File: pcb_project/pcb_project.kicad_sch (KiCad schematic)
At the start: 0 parts

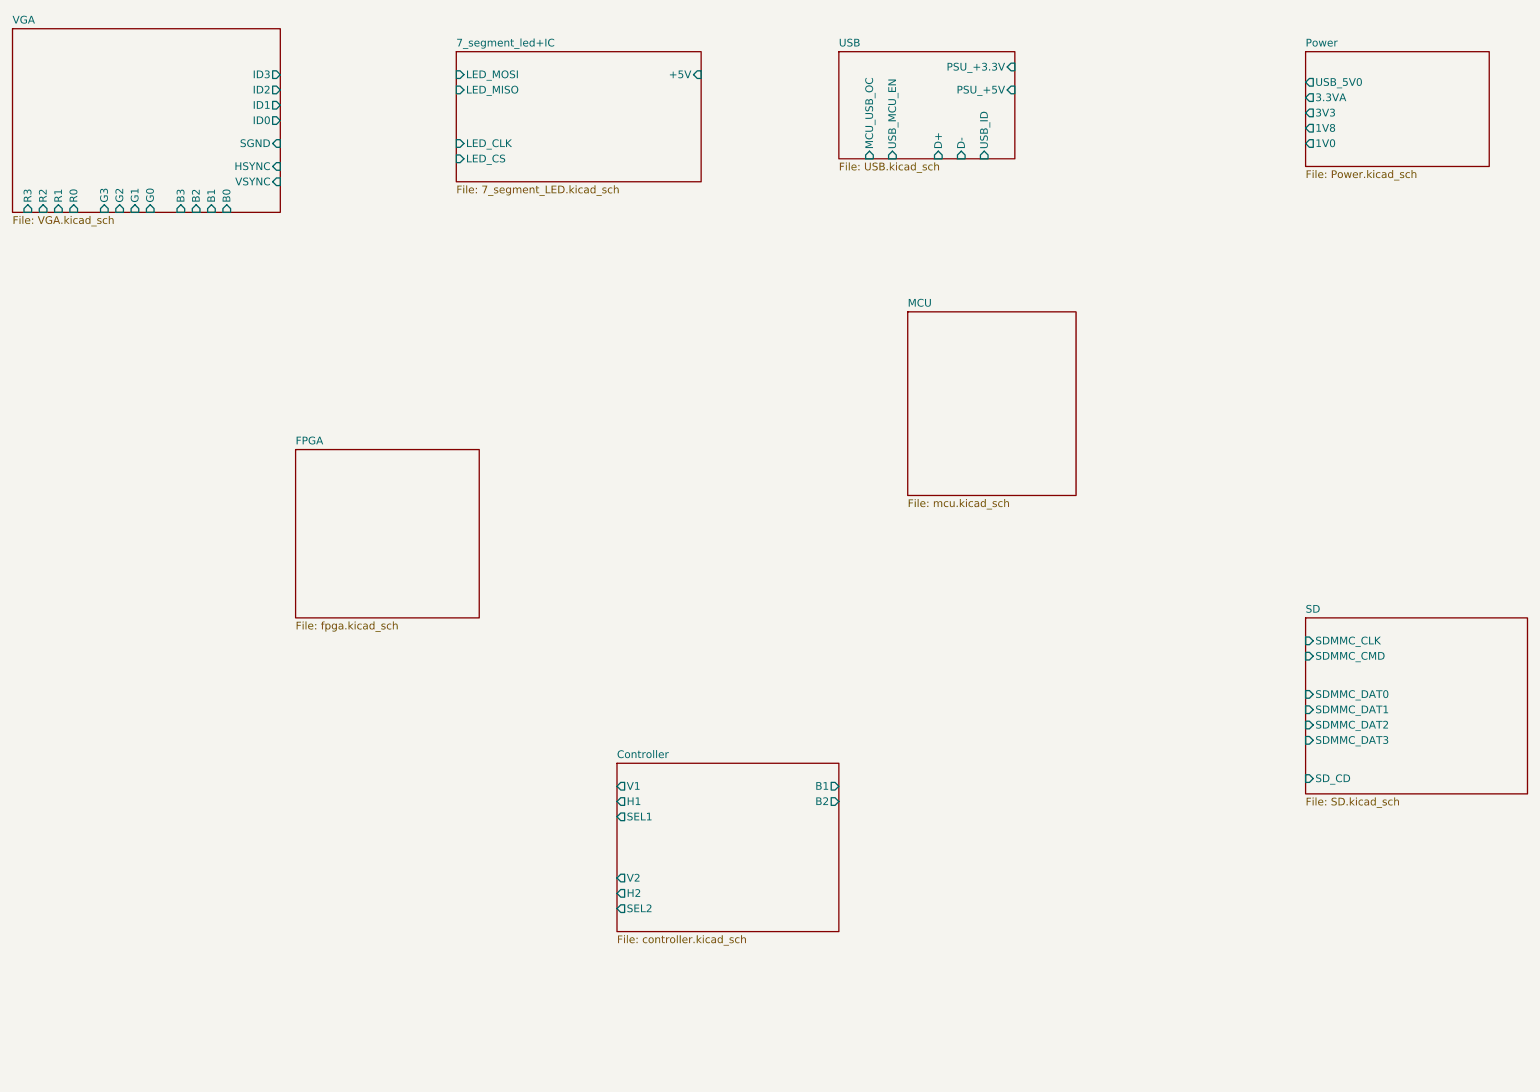
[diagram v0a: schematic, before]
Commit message: Connect Controller, LED-display, USB and SD reader to MCU
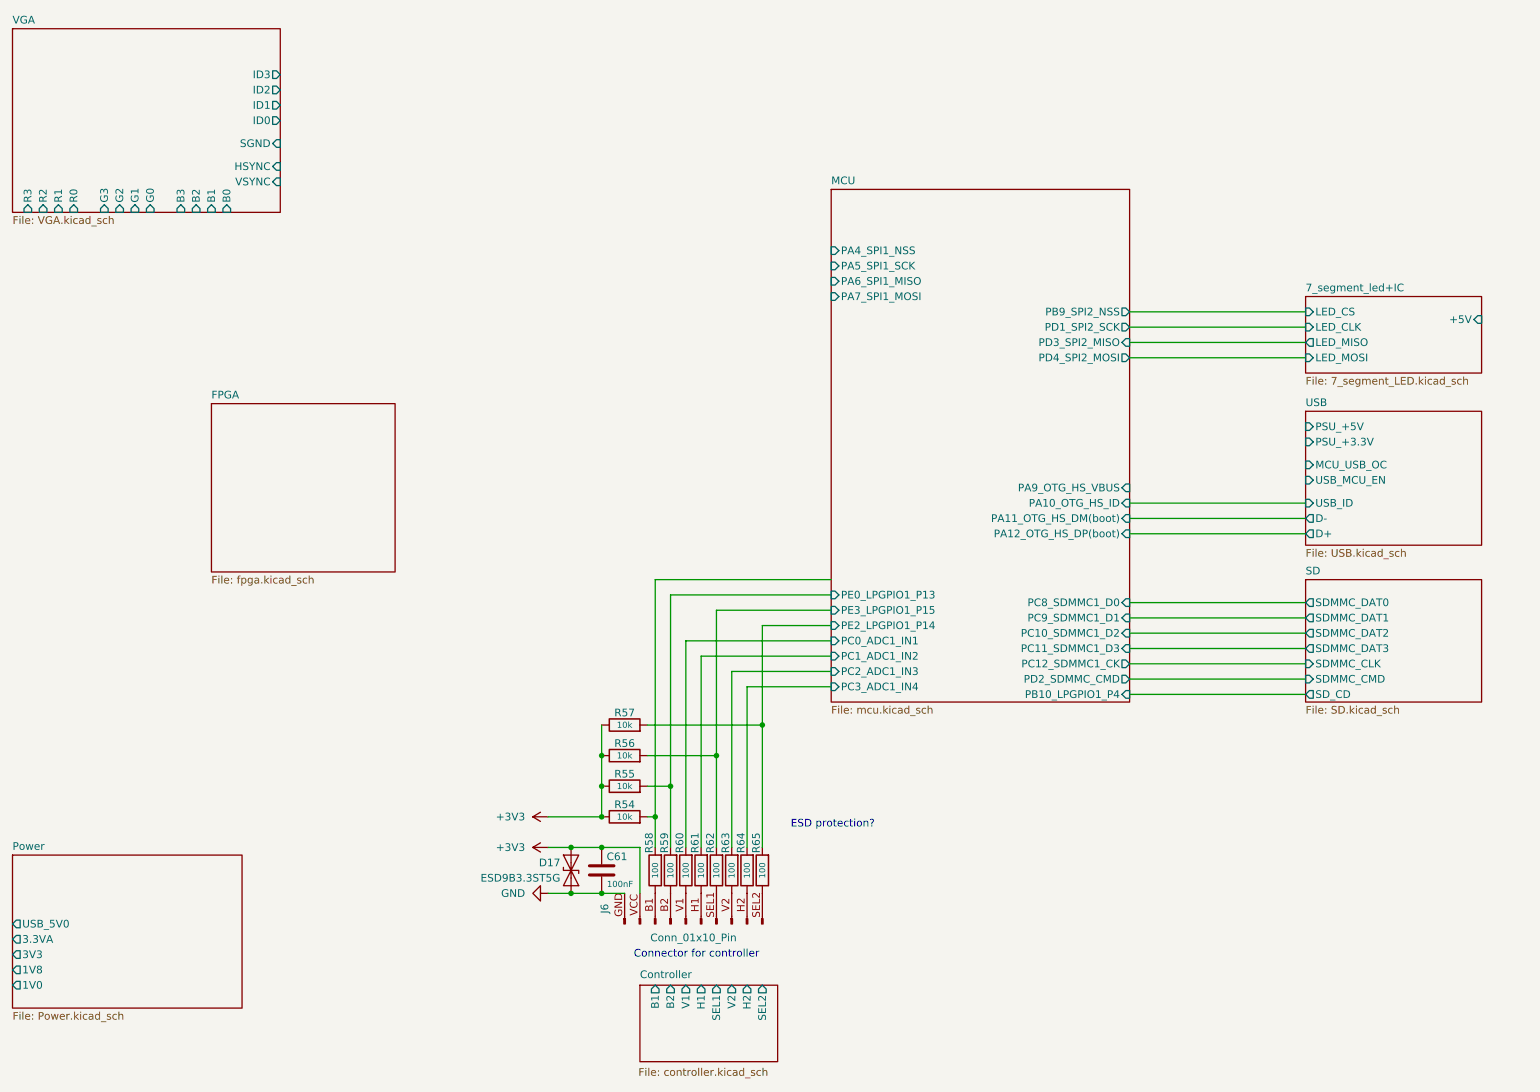
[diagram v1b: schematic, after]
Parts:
- added C61: 100nF, symbol Device:C
- added D17: ESD9B3.3ST5G, Diode_SMD:D_SOD-923, symbol Diode:ESD9B3.3ST5G
- added J6: Conn_01x10_Pin, symbol Connector:Conn_01x10_Pin
- added R54, R55, R56, R57: 10k, symbol Device:R
- added R58, R59, R60, R61, R62, R63, R64, R65: 100, symbol Device:R
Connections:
- new net: J6.B1 (Pin_3), R58.1
- new net: R54.2, R58.2
- new net: J6.B2 (Pin_4), R59.1
- new net: J6.H1 (Pin_6), R61.1
- new net: J6.SEL2 (Pin_10), R65.1
- new net: J6.H2 (Pin_9), R64.1
- new net: J6.SEL1 (Pin_7), R62.1
- new net: J6.V1 (Pin_5), R60.1
- new net: J6.V2 (Pin_8), R63.1
- new net +3V3: C61.1, D17.1 (A1), J6.VCC (Pin_2), R54.1, R55.1, R56.1, R57.1
- new net GND: C61.2, D17.2 (A2), J6.GND (Pin_1)
- new net MCU/PC0_ADC1_IN1: R60.2
- new net MCU/PC1_ADC1_IN2: R61.2
- new net MCU/PC2_ADC1_IN3: R63.2
- new net MCU/PC3_ADC1_IN4: R64.2
- new net MCU/PE0_LPGPIO1_P13: R55.2, R59.2
- new net MCU/PE2_LPGPIO1_P14: R57.2, R65.2
- new net MCU/PE3_LPGPIO1_P15: R56.2, R62.2
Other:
- sheet MCU ports: added PA10_OTG_HS_ID, PA11_OTG_HS_DM(boot), PA12_OTG_HS_DP(boot), PA4_SPI1_NSS, PA5_SPI1_SCK, PA6_SPI1_MISO, PA7_SPI1_MOSI, PA9_OTG_HS_VBUS, PB10_LPGPIO1_P4, PB9_SPI2_NSS, PC0_ADC1_IN1, PC10_SDMMC1_D2, PC11_SDMMC1_D3, PC12_SDMMC1_CK, PC1_ADC1_IN2, PC2_ADC1_IN3, PC3_ADC1_IN4, PC8_SDMMC1_D0, PC9_SDMMC1_D1, PD1_SPI2_SCK, PD2_SDMMC_CMD, PD3_SPI2_MISO, PD4_SPI2_MOSI, PE0_LPGPIO1_P13, PE2_LPGPIO1_P14, PE3_LPGPIO1_P15; removed none
- note added: "Connector for controller"
- note added: "ESD protection?"

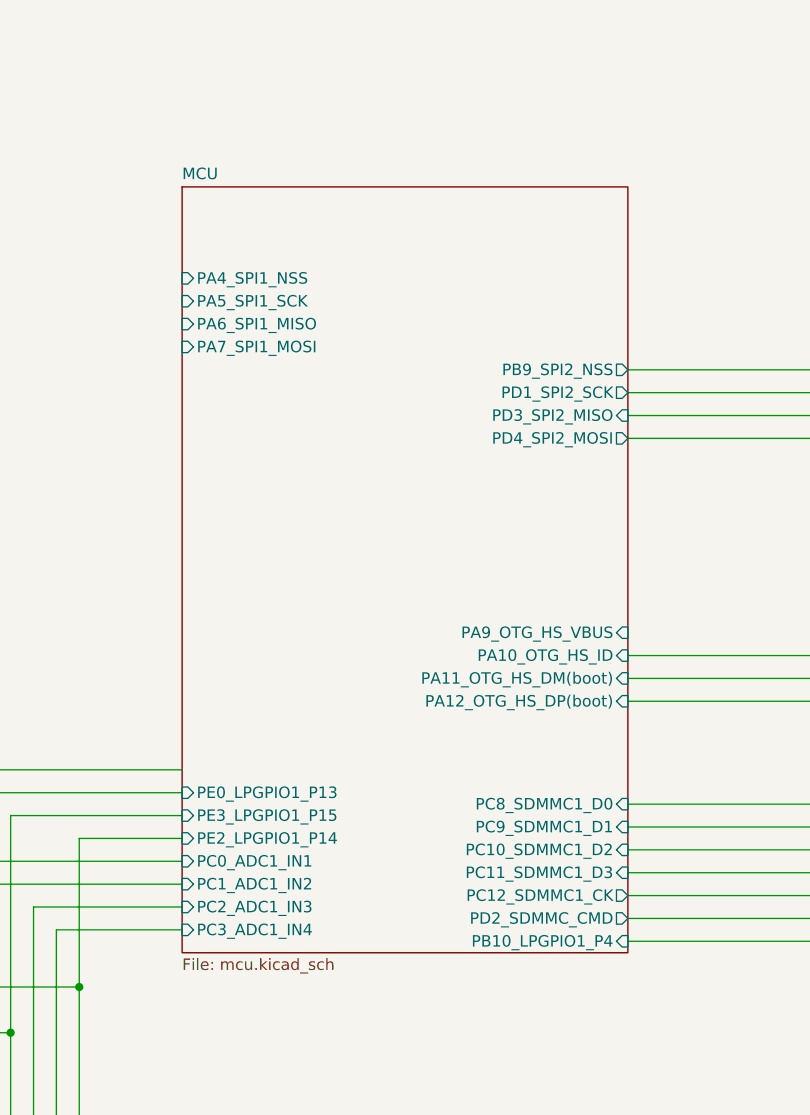
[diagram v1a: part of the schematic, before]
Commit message: Setup pins for OCTOSPI
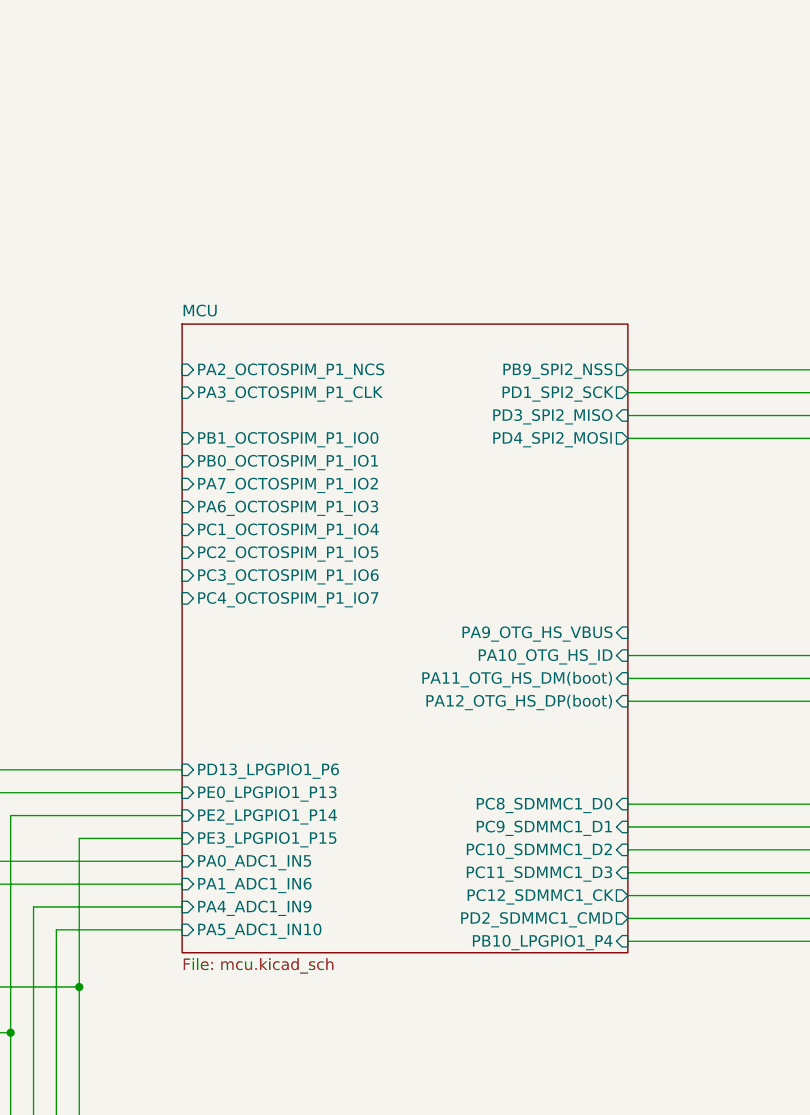
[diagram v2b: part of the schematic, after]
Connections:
- net MCU/PE2_LPGPIO1_P14: now also R56.2, R62.2; no longer R57.2, R65.2
- net MCU/PE3_LPGPIO1_P15: now also R57.2, R65.2; no longer R56.2, R62.2
- net MCU/PD13_LPGPIO1_P6: now reaches R54.2, R58.2
- net MCU/PC0_ADC1_IN1 renamed MCU/PA0_ADC1_IN5
- net MCU/PC1_ADC1_IN2 renamed MCU/PA1_ADC1_IN6
- net MCU/PC2_ADC1_IN3 renamed MCU/PA4_ADC1_IN9
- net MCU/PC3_ADC1_IN4 renamed MCU/PA5_ADC1_IN10
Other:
- sheet MCU ports: added PA0_ADC1_IN5, PA1_ADC1_IN6, PA2_OCTOSPIM_P1_NCS, PA3_OCTOSPIM_P1_CLK, PA4_ADC1_IN9, PA5_ADC1_IN10, PA6_OCTOSPIM_P1_IO3, PA7_OCTOSPIM_P1_IO2, PB0_OCTOSPIM_P1_IO1, PB1_OCTOSPIM_P1_IO0, PC1_OCTOSPIM_P1_IO4, PC2_OCTOSPIM_P1_IO5, PC3_OCTOSPIM_P1_IO6, PC4_OCTOSPIM_P1_IO7, PD13_LPGPIO1_P6, PD2_SDMMC1_CMD; removed PA4_SPI1_NSS, PA5_SPI1_SCK, PA6_SPI1_MISO, PA7_SPI1_MOSI, PC0_ADC1_IN1, PC1_ADC1_IN2, PC2_ADC1_IN3, PC3_ADC1_IN4, PD2_SDMMC_CMD
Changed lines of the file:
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@@
 	)
 	(sheet
-		(at 161.29 49.53)
-		(size 49.53 85.09)
+		(at 161.29 64.77)
+		(size 49.53 69.85)
 		(exclude_from_sim no)
 		(in_bom yes)
@@
 		)
 		(property "Sheetname" "MCU"
-			(at 161.29 48.8184 0)
+			(at 161.29 64.0584 0)
 			(effects
 				(font
@@
 			)
 		)
-		(pin "PD2_SDMMC_CMD" output
-			(at 210.82 130.81 0)
-			(effects
-				(font
-					(size 1.27 1.27)
-				)
-				(justify right)
-			)
-		)
-		(pin "PC3_ADC1_IN4" input
-			(at 161.29 132.08 180)
-			(effects
-				(font
-					(size 1.27 1.27)
-				)
-				(justify left)
-			)
-		)
-		(pin "PC2_ADC1_IN3" input
-			(at 161.29 129.54 180)
-			(effects
-				(font
-					(size 1.27 1.27)
-				)
-				(justify left)
-			)
-		)
-		(pin "PC1_ADC1_IN2" input
-			(at 161.29 127 180)
-			(effects
-				(font
-					(size 1.27 1.27)
-				)
-				(justify left)
-			)
-		)
-		(pin "PC0_ADC1_IN1" input
-			(at 161.29 124.46 180)
-			(effects
-				(font
-					(size 1.27 1.27)
-				)
-				(justify left)
-			)
-		)
 		(pin "PB10_LPGPIO1_P4" input
 			(at 210.82 133.35 0)
@@
 			)
 		)
-		(pin "PA4_SPI1_NSS" input
-			(at 161.29 59.69 180)
-			(effects
-				(font
-					(size 1.27 1.27)
-				)
-				(justify left)
-			)
-		)
-		(pin "PA5_SPI1_SCK" input
-			(at 161.29 62.23 180)
-			(effects
-				(font
-					(size 1.27 1.27)
-				)
-				(justify left)
-			)
-		)
-		(pin "PA6_SPI1_MISO" input
-			(at 161.29 64.77 180)
-			(effects
-				(font
-					(size 1.27 1.27)
-				)
-				(justify left)
-			)
-		)
-		(pin "PA7_SPI1_MOSI" input
-			(at 161.29 67.31 180)
-			(effects
-				(font
-					(size 1.27 1.27)
-				)
-				(justify left)
-			)
-		)
 		(pin "PE0_LPGPIO1_P13" input
 			(at 161.29 116.84 180)
@@
 			)
 		)
+		(pin "PA2_OCTOSPIM_P1_NCS" input
+			(at 161.29 69.85 180)
+			(effects
+				(font
+					(size 1.27 1.27)
+				)
+				(justify left)
+			)
+		)
+		(pin "PA3_OCTOSPIM_P1_CLK" input
+			(at 161.29 72.39 180)
+			(effects
+				(font
+					(size 1.27 1.27)
+				)
+				(justify left)
+			)
+		)
+		(pin "PB0_OCTOSPIM_P1_IO1" input
+			(at 161.29 80.01 180)
+			(effects
+				(font
+					(size 1.27 1.27)
+				)
+				(justify left)
+			)
+		)
+		(pin "PB1_OCTOSPIM_P1_IO0" input
+			(at 161.29 77.47 180)
+			(effects
+				(font
+					(size 1.27 1.27)
+				)
+				(justify left)
+			)
+		)
+		(pin "PA6_OCTOSPIM_P1_IO3" input
+			(at 161.29 85.09 180)
+			(effects
+				(font
+					(size 1.27 1.27)
+				)
+				(justify left)
+			)
+		)
+		(pin "PA7_OCTOSPIM_P1_IO2" input
+			(at 161.29 82.55 180)
+			(effects
+				(font
+					(size 1.27 1.27)
+				)
+				(justify left)
+			)
+		)
+		(pin "PA5_ADC1_IN10" input
+			(at 161.29 132.08 180)
+			(effects
+				(font
+					(size 1.27 1.27)
+				)
+				(justify left)
+			)
+		)
+		(pin "PA4_ADC1_IN9" input
+			(at 161.29 129.54 180)
+			(effects
+				(font
+					(size 1.27 1.27)
+				)
+				(justify left)
+			)
+		)
+		(pin "PA1_ADC1_IN6" input
+			(at 161.29 127 180)
+			(effects
+				(font
+					(size 1.27 1.27)
+				)
+				(justify left)
+			)
+		)
+		(pin "PA0_ADC1_IN5" input
+			(at 161.29 124.46 180)
+			(effects
+				(font
+					(size 1.27 1.27)
+				)
+				(justify left)
+			)
+		)
+		(pin "PC2_OCTOSPIM_P1_IO5" input
+			(at 161.29 90.17 180)
+			(effects
+				(font
+					(size 1.27 1.27)
+				)
+				(justify left)
+			)
+		)
+		(pin "PC4_OCTOSPIM_P1_IO7" input
+			(at 161.29 95.25 180)
+			(effects
+				(font
+					(size 1.27 1.27)
+				)
+				(justify left)
+			)
+		)
+		(pin "PC3_OCTOSPIM_P1_IO6" input
+			(at 161.29 92.71 180)
+			(effects
+				(font
+					(size 1.27 1.27)
+				)
+				(justify left)
+			)
+		)
+		(pin "PC1_OCTOSPIM_P1_IO4" input
+			(at 161.29 87.63 180)
+			(effects
+				(font
+					(size 1.27 1.27)
+				)
+				(justify left)
+			)
+		)
+		(pin "PD13_LPGPIO1_P6" input
+			(at 161.29 114.3 180)
+			(effects
+				(font
+					(size 1.27 1.27)
+				)
+				(justify left)
+			)
+		)
 		(pin "PE3_LPGPIO1_P15" input
+			(at 161.29 121.92 180)
+			(effects
+				(font
+					(size 1.27 1.27)
+				)
+				(justify left)
+			)
+		)
+		(pin "PE2_LPGPIO1_P14" input
 			(at 161.29 119.38 180)
 			(effects
@@
 			)
 		)
-		(pin "PE2_LPGPIO1_P14" input
-			(at 161.29 121.92 180)
-			(effects
-				(font
-					(size 1.27 1.27)
-				)
-				(justify left)
-			)
-		)
+		(pin "PD2_SDMMC1_CMD" output
+			(at 210.82 130.81 0)
+			(effects
+				(font
+					(size 1.27 1.27)
+				)
+				(justify right)
+			)
+		)

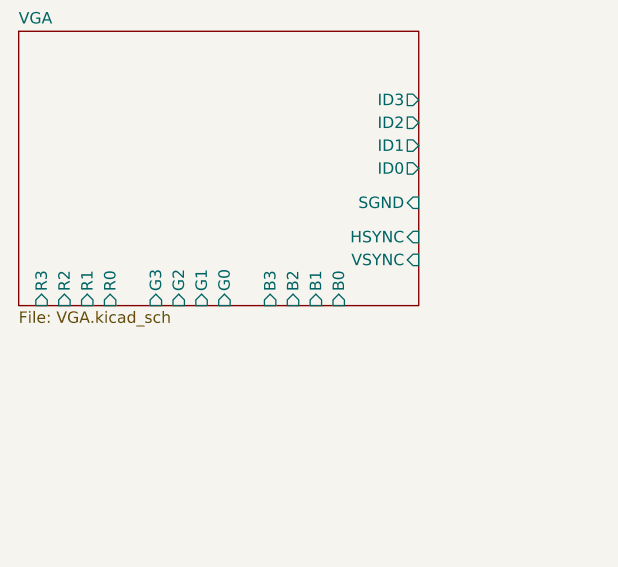
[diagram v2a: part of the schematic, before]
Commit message: Add pin placement for OSPI on FPGA, not wired in root yet
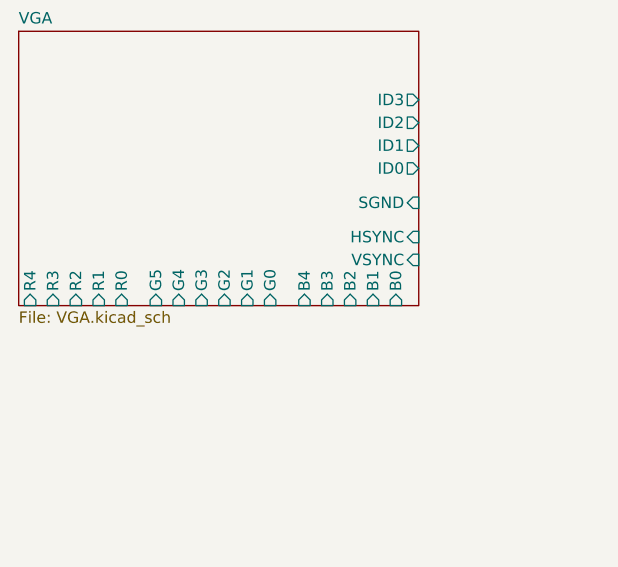
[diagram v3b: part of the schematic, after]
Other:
- sheet VGA ports: added B4, G4, G5, R4; removed none
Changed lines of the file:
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@@
 		)
 		(pin "B0" input
-			(at 60.96 53.34 270)
+			(at 67.31 53.34 270)
 			(effects
 				(font
@@
 		)
 		(pin "B2" input
-			(at 55.88 53.34 270)
+			(at 62.23 53.34 270)
 			(effects
 				(font
@@
 		)
 		(pin "R3" input
-			(at 27.94 53.34 270)
+			(at 29.21 53.34 270)
 			(effects
 				(font
@@
 		)
 		(pin "R0" input
-			(at 35.56 53.34 270)
+			(at 36.83 53.34 270)
 			(effects
 				(font
@@
 		)
 		(pin "B3" input
-			(at 53.34 53.34 270)
+			(at 59.69 53.34 270)
 			(effects
 				(font
@@
 		)
 		(pin "G3" input
-			(at 40.64 53.34 270)
+			(at 45.72 53.34 270)
 			(effects
 				(font
@@
 		)
 		(pin "G1" input
-			(at 45.72 53.34 270)
+			(at 50.8 53.34 270)
 			(effects
 				(font
@@
 		)
 		(pin "G2" input
-			(at 43.18 53.34 270)
+			(at 48.26 53.34 270)
 			(effects
 				(font
@@
 		)
 		(pin "R1" input
-			(at 33.02 53.34 270)
+			(at 34.29 53.34 270)
 			(effects
 				(font
@@
 		)
 		(pin "R2" input
-			(at 30.48 53.34 270)
+			(at 31.75 53.34 270)
 			(effects
 				(font
@@
 		)
 		(pin "G0" input
-			(at 48.26 53.34 270)
+			(at 53.34 53.34 270)
 			(effects
 				(font
@@
 		)
 		(pin "B1" input
-			(at 58.42 53.34 270)
-			(effects
-				(font
+			(at 64.77 53.34 270)
+			(effects
+				(font
+					(size 1.27 1.27)
+				)
+				(justify left)
+			)
+		)
+		(pin "B4" input
+			(at 57.15 53.34 270)
+			(effects
+				(font
+					(size 1.27 1.27)
+				)
+				(justify left)
+			)
+		)
+		(pin "G4" input
+			(at 43.18 53.34 270)
+			(effects
+				(font
+					(size 1.27 1.27)
+				)
+				(justify left)
+			)
+		)
+		(pin "G5" input
+			(at 40.64 53.34 270)
+			(effects
+				(font
+					(size 1.27 1.27)
+				)
+				(justify left)
+			)
+		)
+		(pin "R4" input
+			(at 26.67 53.34 270)
+			(effects
+				(font
